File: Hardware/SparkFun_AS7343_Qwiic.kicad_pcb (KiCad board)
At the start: 2 copper layers, 25.4 x 25.4 mm, 64 parts, among them J1 Qwiic_RA, J2 Qwiic_RA, J3 Conn_01x06, Q1 BSS138, Q2 BSS138, U1 RT9080-1.8V, U2 AS7343

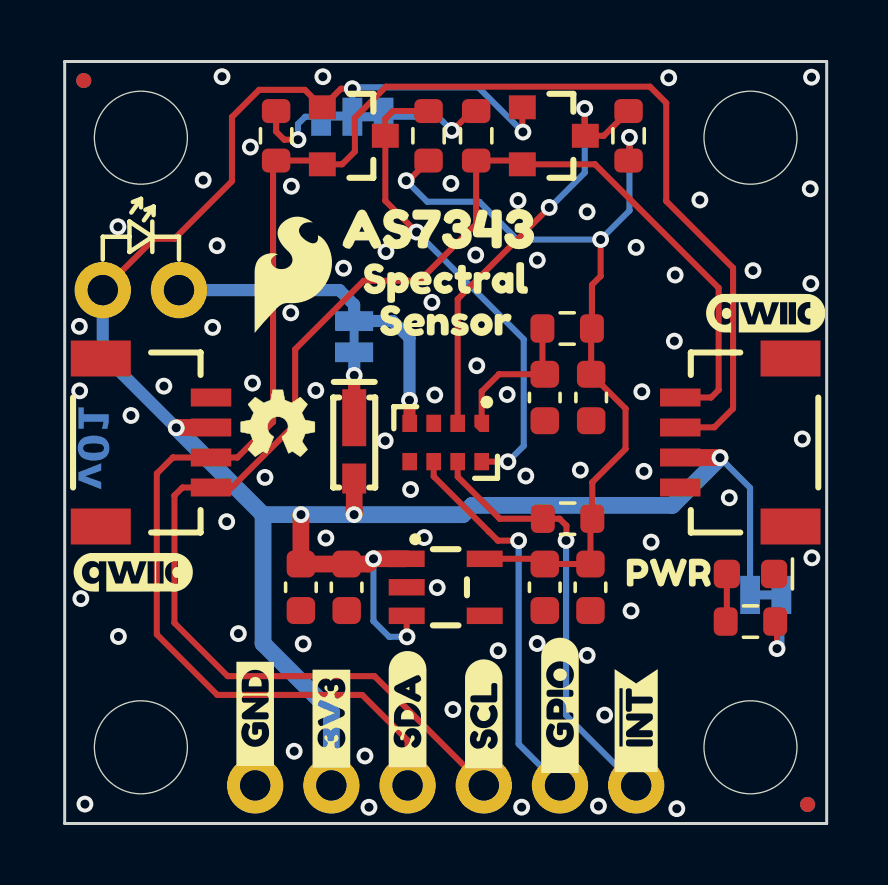
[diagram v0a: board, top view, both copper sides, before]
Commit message: more review notes
-changed 1V8 to 1.8V to match style of 3.3V
-corrected schematic note for low pass filter. Is kHz, was KHz
-removed one of the QWIIC logos
-Moved OSHW to bottom silk
-aligned PWR LED silk label exactly with Y val of LED.
-changed sch note about i2c address to be "7-bit unshifted I2C address: 0x39"
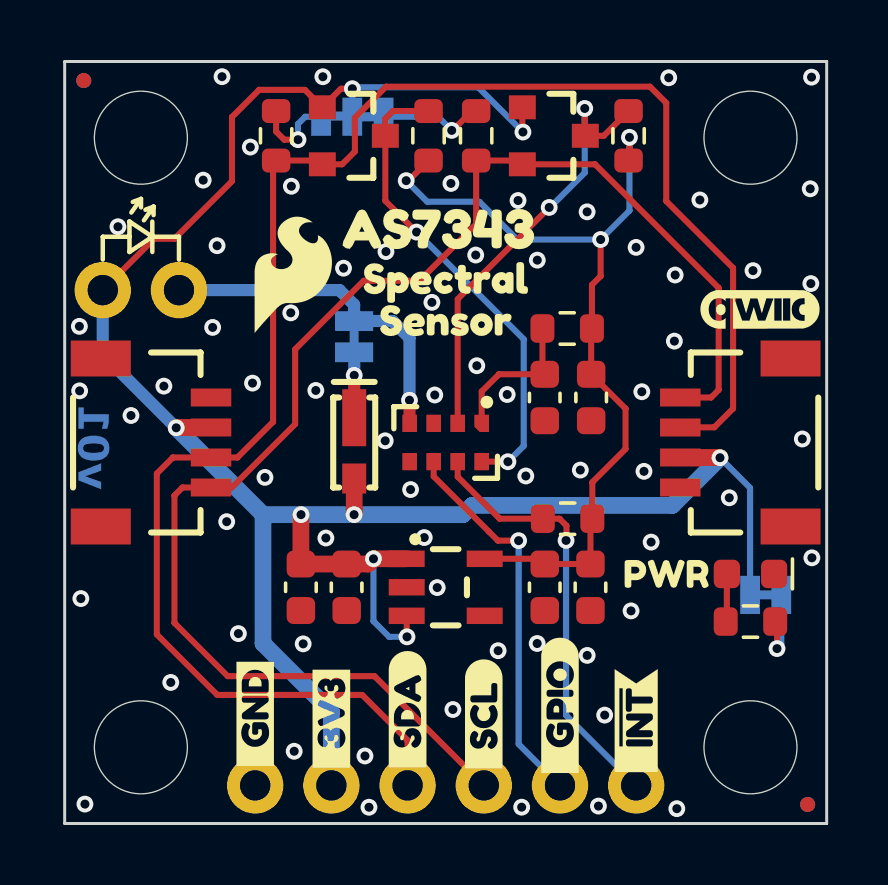
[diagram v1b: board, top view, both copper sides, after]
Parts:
- removed the G*** at (125.6, 102.4)
- Ref**: moved to B.Cu
- moved Ref** 8.24 mm to (125.8, 104.5), turned to 180 degrees
- moved G*** 0.23 mm to (146.4, 93.7)
- moved kibuzzard-65A8A8B4 0.08 mm to (143.3, 102.5)
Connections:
- net 1V8 renamed 1.8V

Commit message: everything moved to 12.5 mil grid
-moved all parts to 12.5 mil grid and re-routed as necessary
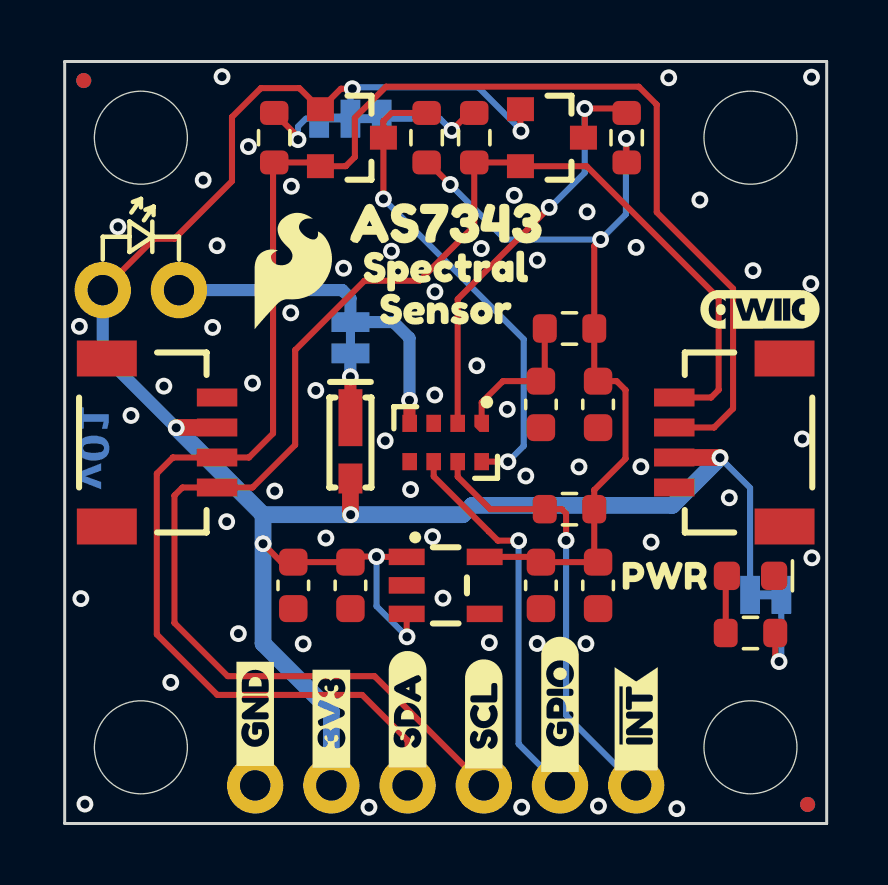
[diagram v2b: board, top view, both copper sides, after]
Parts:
- removed kibuzzard-67D9D97F: G***, kibuzzard-67D9D97F
- removed kibuzzard-67D9E7C1: G***, kibuzzard-67D9E7C1
- added kibuzzard-67F8112D: G***, kibuzzard-67F8112D, B.Cu at (129.6, 87.3)
- added kibuzzard-67F81140: G***, kibuzzard-67F81140, B.Cu at (143.9, 103.2)
- moved kibuzzard-67ED66F3 0.46 mm to (141.7, 96.8)
- moved kibuzzard-67ED66FD 0.46 mm to (141.7, 98.1)
- moved G*** 0.40 mm to (141.7, 100.0)
- moved R3 0.38 mm to (146.1, 104.5)
- moved kibuzzard-67ED66F3 0.38 mm to (136.0, 92.4)
- moved kibuzzard-67ED66FD 0.38 mm to (136.0, 93.7)
- moved C4 0.33 mm to (141.0, 96.8)
- moved R2 0.32 mm to (140.1, 100.3)
- moved kibuzzard-67ED66D1 0.32 mm to (136.0, 90.8)
- moved C3 0.26 mm to (139.1, 96.8)
- moved C5 0.26 mm to (130.9, 102.9)
- moved C6 0.26 mm to (141.0, 102.9)
- moved kibuzzard-67F027E1 0.22 mm to (132.4, 102.6)
- moved J1 0.20 mm to (143.6, 98.1)
- moved J2 0.20 mm to (128.3, 98.1)
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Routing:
- net 1.8V: track 28.4 -> 27.4 mm
- net GND: vias 67 -> 55

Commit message: eng checklist for protos v01
-solder mask changed to black for protos
-DRC exclusions
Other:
- board text added: "Solder Mask: Black"
- board text removed: "Solder Mask: Red"
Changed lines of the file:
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@@
 		)
 	)
-	(gr_text "Solder Mask: Red"
+	(gr_text "Solder Mask: Black"
 		(at 198.354 145.232 0)
 		(layer "Eco1.User")

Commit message: added USER LED label to bottom silk
-changed value ot D3 to "USER"
-added silk label to bottom for USER LED
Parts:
- added kibuzzard-67F954F3: G***, kibuzzard-67F954F3, B.Cu at (125.8, 91.4)
- D3: value LED -> USER
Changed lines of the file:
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@@
 			)
 		)
-		(property "Value" "LED"
+		(property "Value" "USER"
 			(at 0 1.27 0)
 			(layer "F.Fab")
@@
 		(embedded_fonts no)
 	)
+	(footprint "kibuzzard-67F954F3"
+		(layer "B.Cu")
+		(at 125.806 91.4385 180)
+		(descr "Generated with KiBuzzard")
+		(tags "kb_params=eyJBbGlnbm1lbnRDaG9pY2UiOiAiQ2VudGVyIiwgIkNhcExlZnRDaG9pY2UiOiAiKCIsICJDYXBSaWdodENob2ljZSI6ICJdIiwgIkZvbnRDb21ib0JveCI6ICJGcmVkZHlTcGFyay1SZWd1bGFyIiwgIkhlaWdodEN0cmwiOiAwLjksICJMYXllckNvbWJvQm94IjogIkYuU2lsa1MiLCAiTGluZVNwYWNpbmdDdHJsIjogMS41LCAiTXVsdGlMaW5lVGV4dCI6ICIoVVNFUikiLCAiUGFkZGluZ0JvdHRvbUN0cmwiOiAxLjAsICJQYWRkaW5nTGVmdEN0cmwiOiAwLjAsICJQYWRkaW5nUmlnaHRDdHJsIjogMC4wLCAiUGFkZGluZ1RvcEN0cmwiOiAxLjAsICJXaWR0aEN0cmwiOiAxLjAsICJhZHZhbmNlZENoZWNrYm94IjogdHJ1ZSwgImlubGluZUZvcm1hdFRleHRib3giOiB0cnVlLCAibGluZW92ZXJTdHlsZUNob2ljZSI6ICJTcXVhcmUiLCAibGluZW92ZXJUaGlja25lc3NDdHJsIjogMX0=")
+		(property "Reference" "kibuzzard-67F954F3"
+			(at 0 3.620103 0)
+			(layer "B.SilkS")
+			(hide yes)
+			(effects
+				(font
+					(size 0.001 0.001)
+				)
+				(justify mirror)
+			)
+		)
+		(property "Value" "G***"
+			(at 0 -3.620103 0)
+			(layer "B.SilkS")
+			(hide yes)
+			(effects
+				(font
+					(size 0.001 0.001)
+				)
+				(justify mirror)
+			)
+		)
+		(property "Datasheet" ""
+			(at 0 0 0)
+			(layer "B.Fab")
+			(hide yes)
+			(effects
+				(font
+					(size 1.27 1.27)
+					(thickness 0.15)
+				)
+				(justify mirror)
+			)
+		)
+		(property "Description" ""
+			(at 0 0 0)
+			(layer "B.Fab")
+			(hide yes)
+			(effects
+				(font
+					(size 1.27 1.27)
+					(thickness 0.15)
+				)
+				(justify mirror)
+			)
+		)
+		(attr board_only exclude_from_pos_files exclude_from_bom)
+		(fp_poly
+			(pts
+				(xy 1.05 0.027039) (xy 1.191631 0.027039) (xy 1.253433 0.050215) (xy 1.283047 0.12103) (xy 1.255365 0.187983)
+				(xy 1.189056 0.215021) (xy 1.05 0.215021) (xy 1.05 0.027039)
+			)
+			(stroke
+				(width 0)
+				(type solid)
+			)
+			(fill yes)
+			(layer "B.SilkS")
+		)
+		(fp_poly
+			(pts
+				(xy -1.537983 0.572103) (xy -1.53809 0.572103) (xy -1.594166 0.569348) (xy -1.649702 0.56111) (xy -1.704163 0.547468)
+				(xy -1.757024 0.528554) (xy -1.807778 0.50455) (xy -1.855934 0.475686) (xy -1.901028 0.442242) (xy -1.942628 0.404538)
+				(xy -1.980332 0.362938) (xy -2.013776 0.317843) (xy -2.04264 0.269687) (xy -2.066644 0.218934) (xy -2.085559 0.166073)
+				(xy -2.0992 0.111612) (xy -2.107438 0.056076) (xy -2.110193 0) (xy -2.107438 -0.056076) (xy -2.0992 -0.111612)
+				(xy -2.085559 -0.166073) (xy -2.066644 -0.218934) (xy -2.04264 -0.269687) (xy -2.013776 -0.317843)
+				(xy -1.980332 -0.362938) (xy -1.942628 -0.404538) (xy -1.901028 -0.442242) (xy -1.855934 -0.475686)
+				(xy -1.807778 -0.50455) (xy -1.757024 -0.528554) (xy -1.704163 -0.547468) (xy -1.649702 -0.56111)
+				(xy -1.594166 -0.569348) (xy -1.53809 -0.572103) (xy -1.537983 -0.572103) (xy -1.141416 -0.572103)
+				(xy -1.141416 -0.464807) (xy -1.231223 -0.454989) (xy -1.312661 -0.425536) (xy -1.382672 -0.379989)
+				(xy -1.438197 -0.321888) (xy -1.480848 -0.254614) (xy -1.512232 -0.181545) (xy -1.531545 -0.104936)
+				(xy -1.537983 -0.027039) (xy -1.537983 0.333476) (xy -1.536052 0.377897) (xy -1.52382 0.413305)
+				(xy -1.487768 0.442918) (xy -1.419528 0.451931) (xy -1.351931 0.442918) (xy -1.316524 0.413948)
+				(xy -1.303648 0.377897) (xy -1.301073 0.332189) (xy -1.301073 -0.027039) (xy -1.288197 -0.117811)
+				(xy -1.236695 -0.193777) (xy -1.192597 -0.219367) (xy -1.137554 -0.227897) (xy -1.071567 -0.214056)
+				(xy -1.020386 -0.172532) (xy -0.987554 -0.108155) (xy -0.976609 -0.025751) (xy -0.976609 0.339914)
+				(xy -0.974034 0.38176) (xy -0.961159 0.415236) (xy -0.925107 0.442918) (xy -0.858155 0.451931) (xy -0.791202 0.442918)
+				(xy -0.75515 0.412661) (xy -0.742918 0.376609) (xy -0.740987 0.332189) (xy -0.740987 -0.029614)
+				(xy -0.747586 -0.107511) (xy -0.767382 -0.18412) (xy -0.79941 -0.257028) (xy -0.842704 -0.32382)
+				(xy -0.898873 -0.381277) (xy -0.969528 -0.42618) (xy -1.051449 -0.45515) (xy -1.141416 -0.464807)
+				(xy -1.141416 -0.572103) (xy -0.356009 -0.572103) (xy -0.356009 -0.463519) (xy -0.428112 -0.457725)
+				(xy -0.488627 -0.443562) (xy -0.538197 -0.422318) (xy -0.578112 -0.397854) (xy -0.609013 -0.372747)
+				(xy -0.631545 -0.350215) (xy -0.645708 -0.332189) (xy -0.653433 -0.323176) (xy -0.685622 -0.239485)
+				(xy -0.631545 -0.157082) (xy -0.57804 -0.127325) (xy -0.522246 -0.135908) (xy -0.464163 -0.182833)
+				(xy -0.412017 -0.229828) (xy -0.361159 -0.24206) (xy -0.285193 -0.223391) (xy -0.262017 -0.163519)
+				(xy -0.295494 -0.123605) (xy -0.396567 -0.093348) (xy -0.457886 -0.07677) (xy -0.506652 -0.059227)
+				(xy -0.578755 -0.018026) (xy -0.630258 0.037339) (xy -0.661159 0.106867) (xy -0.671459 0.190558)
+				(xy -0.661874 0.265021) (xy -0.633119 0.330472) (xy -0.585193 0.38691) (xy -0.522675 0.430186) (xy -0.450143 0.456152)
+				(xy -0.367597 0.464807) (xy -0.270458 0.456223) (xy -0.188484 0.430472) (xy -0.121674 0.387554)
+				(xy -0.075322 0.321245) (xy -0.106223 0.24206) (xy -0.182189 0.179614) (xy -0.268455 0.203433) (xy -0.283262 0.215665)
+				(xy -0.301288 0.230472) (xy -0.326395 0.240129) (xy -0.368884 0.244635) (xy -0.416524 0.228541)
+				(xy -0.437124 0.18927) (xy -0.414592 0.147425) (xy -0.363734 0.124893) (xy -0.285193 0.108798) (xy -0.20279 0.088841)
+				(xy -0.129882 0.055365) (xy -0.073391 0.006438) (xy -0.037178 -0.063412) (xy -0.025107 -0.159657)
+				(xy -0.030579 -0.221137) (xy -0.046996 -0.276824) (xy -0.103004 -0.363734) (xy -0.182189 -0.42103)
+				(xy -0.270386 -0.453863) (xy -0.356009 -0.463519) (xy -0.356009 -0.572103) (xy 0.159013 -0.572103)
+				(xy 0.159013 -0.450644) (xy 0.09206 -0.441631) (xy 0.056009 -0.412017) (xy 0.043777 -0.376609) (xy 0.041845 -0.332189)
+				(xy 0.041845 0.333476) (xy 0.06824 0.425536) (xy 0.162876 0.450644) (xy 0.63412 0.450644) (xy 0.678541 0.448712)
+				(xy 0.713305 0.436481) (xy 0.742275 0.400429) (xy 0.751288 0.332189) (xy 0.742275 0.265236) (xy 0.712661 0.229185)
+				(xy 0.677253 0.216953) (xy 0.632833 0.215021) (xy 0.277468 0.215021) (xy 0.277468 0.100429) (xy 0.515665 0.100429)
+				(xy 0.557511 0.098498) (xy 0.588412 0.088197) (xy 0.612876 0.057296) (xy 0.619957 -0.001288) (xy 0.612876 -0.058584)
+				(xy 0.587768 -0.088197) (xy 0.555579 -0.098498) (xy 0.51309 -0.100429) (xy 0.277468 -0.100429) (xy 0.277468 -0.215021)
+				(xy 0.63412 -0.215021) (xy 0.678541 -0.216953) (xy 0.713305 -0.229185) (xy 0.742275 -0.265236) (xy 0.751288 -0.333476)
+				(xy 0.742275 -0.400429) (xy 0.712661 -0.436481) (xy 0.677253 -0.448712) (xy 0.632833 -0.450644)
+				(xy 0.159013 -0.450644) (xy 0.159013 -0.572103) (xy 1.379614 -0.572103) (xy 1.379614 -0.453863)
+				(xy 1.307511 -0.393991) (xy 1.169742 -0.207296) (xy 1.05 -0.207296) (xy 1.05 -0.332189) (xy 1.048069 -0.376609)
+				(xy 1.035837 -0.411373) (xy 0.999785 -0.440343) (xy 0.931545 -0.449356) (xy 0.864592 -0.440343)
+				(xy 0.828541 -0.41073) (xy 0.816309 -0.375322) (xy 0.814378 -0.330901) (xy 0.814378 0.333476) (xy 0.816309 0.376609)
+				(xy 0.828541 0.412017) (xy 0.864592 0.441631) (xy 0.932833 0.450644) (xy 1.191631 0.450644) (xy 1.243938 0.445494)
+				(xy 1.297854 0.430043) (xy 1.351609 0.404936) (xy 1.403433 0.370815) (xy 1.449624 0.325268) (xy 1.486481 0.26588)
+				(xy 1.510622 0.196191) (xy 1.51867 0.119742) (xy 1.50608 0.023319) (xy 1.468312 -0.059943) (xy 1.405365 -0.130043)
+				(xy 1.498069 -0.253648) (xy 1.532833 -0.342489) (xy 1.47103 -0.418455) (xy 1.379614 -0.453863) (xy 1.379614 -0.572103)
+				(xy 1.537983 -0.572103) (xy 1.53809 -0.572103) (xy 1.594166 -0.569348) (xy 1.649702 -0.56111) (xy 1.704163 -0.547468)
+				(xy 1.757024 -0.528554) (xy 1.807778 -0.50455) (xy 1.855934 -0.475686) (xy 1.901028 -0.442242) (xy 1.942628 -0.404538)
+				(xy 1.980332 -0.362938) (xy 2.013776 -0.317843) (xy 2.04264 -0.269687) (xy 2.066644 -0.218934) (xy 2.085559 -0.166073)
+				(xy 2.0992 -0.111612) (xy 2.107438 -0.056076) (xy 2.110193 0) (xy 2.107438 0.056076) (xy 2.0992 0.111612)
+				(xy 2.085559 0.166073) (xy 2.066644 0.218934) (xy 2.04264 0.269687) (xy 2.013776 0.317843) (xy 1.980332 0.362938)
+				(xy 1.942628 0.404538) (xy 1.901028 0.442242) (xy 1.855934 0.475686) (xy 1.807778 0.50455) (xy 1.757024 0.528554)
+				(xy 1.704163 0.547468) (xy 1.649702 0.56111) (xy 1.594166 0.569348) (xy 1.53809 0.572103) (xy 1.537983 0.572103)
+				(xy -1.537983 0.572103)
+			)
+			(stroke
+				(width 0)
+				(type solid)
+			)
+			(fill yes)
+			(layer "B.SilkS")
+		)
+		(embedded_fonts no)
+	)
 	(footprint "kibuzzard-67F027E1"
 		(layer "B.Cu")
@@
 	)
 	(via
-		(at 125.042 90.914)
+		(at 124.536 90.1685)
 		(size 0.56)
 		(drill 0.3)
